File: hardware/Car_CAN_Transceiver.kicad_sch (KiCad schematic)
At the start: 9 parts, among them IC1 TCAN3413DR

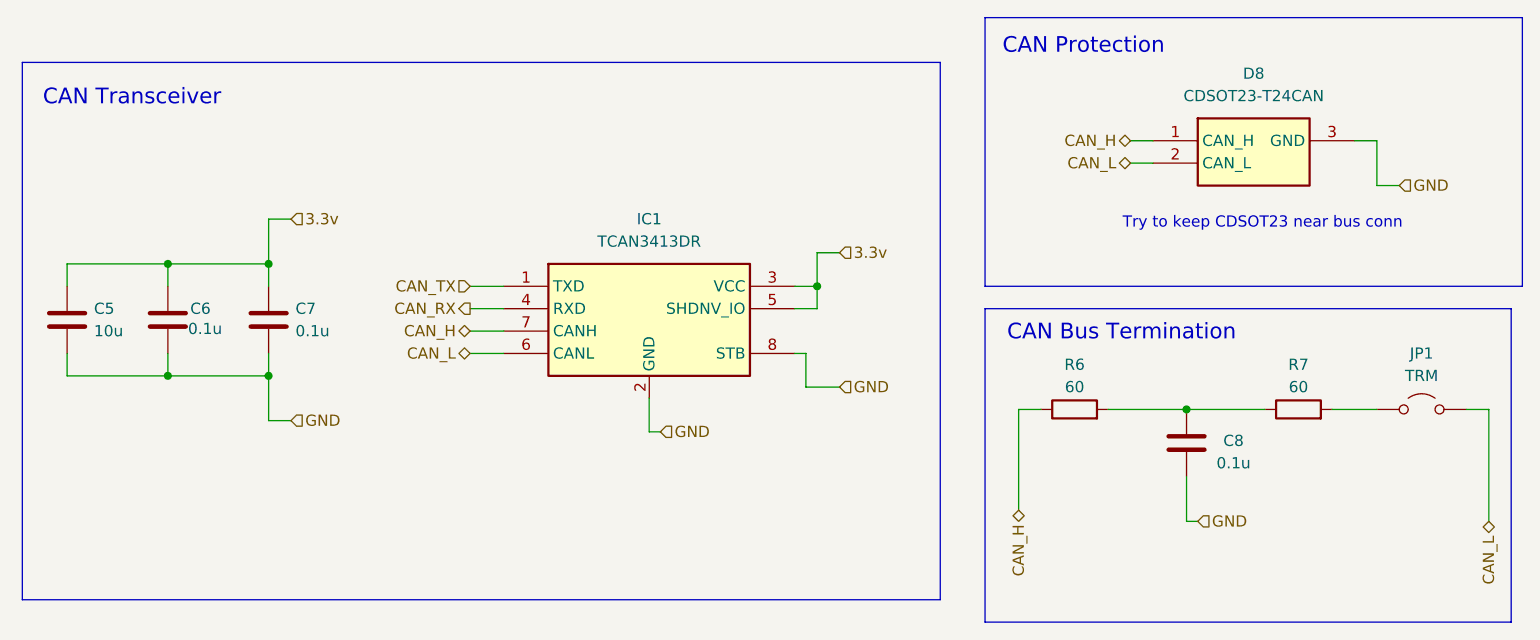
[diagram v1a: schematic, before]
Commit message: finished schematic except for 12v buck boost
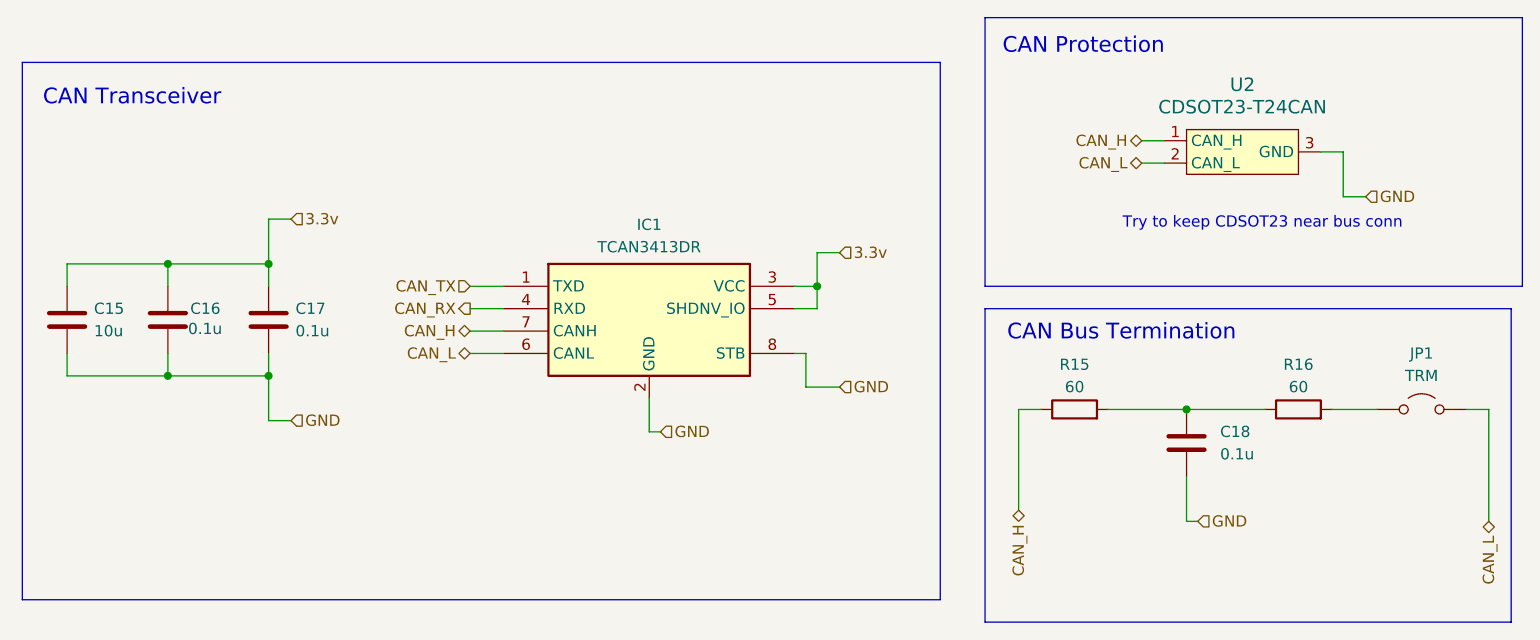
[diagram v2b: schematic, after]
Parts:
- removed C5: 10u, Capacitor_SMD:C_0805_2012Metric_Pad1.18x1.45mm_HandSolder, symbol Device:C
- removed C6, C7: 0.1u, Capacitor_SMD:C_0603_1608Metric_Pad1.08x0.95mm_HandSolder, symbol Device:C
- removed C8: 0.1u, Capacitor_SMD:C_0603_1608Metric_Pad1.08x0.95mm_HandSolder, symbol ECE319K:C
- removed D8: CDSOT23-T24CAN, UTSVT_Passives:CDSOT23-T24CAN, symbol CDSOT23-T24CAN:CDSOT23-T24CAN
- removed IC1: TCAN3413DR, UTSVT_Passives:TCAN3413DR, symbol TCAN3413DR:TCAN3413DR
- removed R7: 60, Resistor_SMD:R_0603_1608Metric_Pad0.98x0.95mm_HandSolder, symbol Device:R
- added C15: 10u, Capacitor_SMD:C_0805_2012Metric_Pad1.18x1.45mm_HandSolder, symbol Device:C
- added C16, C17: 0.1u, Capacitor_SMD:C_0603_1608Metric_Pad1.08x0.95mm_HandSolder, symbol Device:C
- added C18: 0.1u, symbol Device:C
- added IC1: TCAN3413DR, LHRS_Passives:TCAN3413DR, symbol lhrs_ics:TCAN3413DR
- added R16: 60, Resistor_SMD:R_0603_1608Metric_Pad0.98x0.95mm_HandSolder, symbol Device:R
- added U2: CDSOT23-T24CAN, LHRS_ICs:CDSOT23-T24CAN, symbol lhrs_ics:CDSOT23-T24CAN
- renumbered R6 to R15
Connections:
- net 3.3v: now also C15.1, C16.1, C17.1, IC1.3 (VCC), IC1.5 (SHDNV_IO)
- net CAN_H: now also IC1.7 (CANH), U2.1 (CAN_H)
- net CAN_L: now also IC1.6 (CANL), U2.2 (CAN_L)
- net CAN_RX: now also IC1.4 (RXD)
- net CAN_TX: now also IC1.1 (TXD)
- net GND: now also C15.2, C16.2, C17.2, C18.2, IC1.2 (GND), IC1.8 (STB), U2.3 (GND)
- net at R15.2: now also C18.1, R16.1
- net at JP1.1 (A): now also R16.2
